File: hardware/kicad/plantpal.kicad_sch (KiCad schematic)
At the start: 0 parts

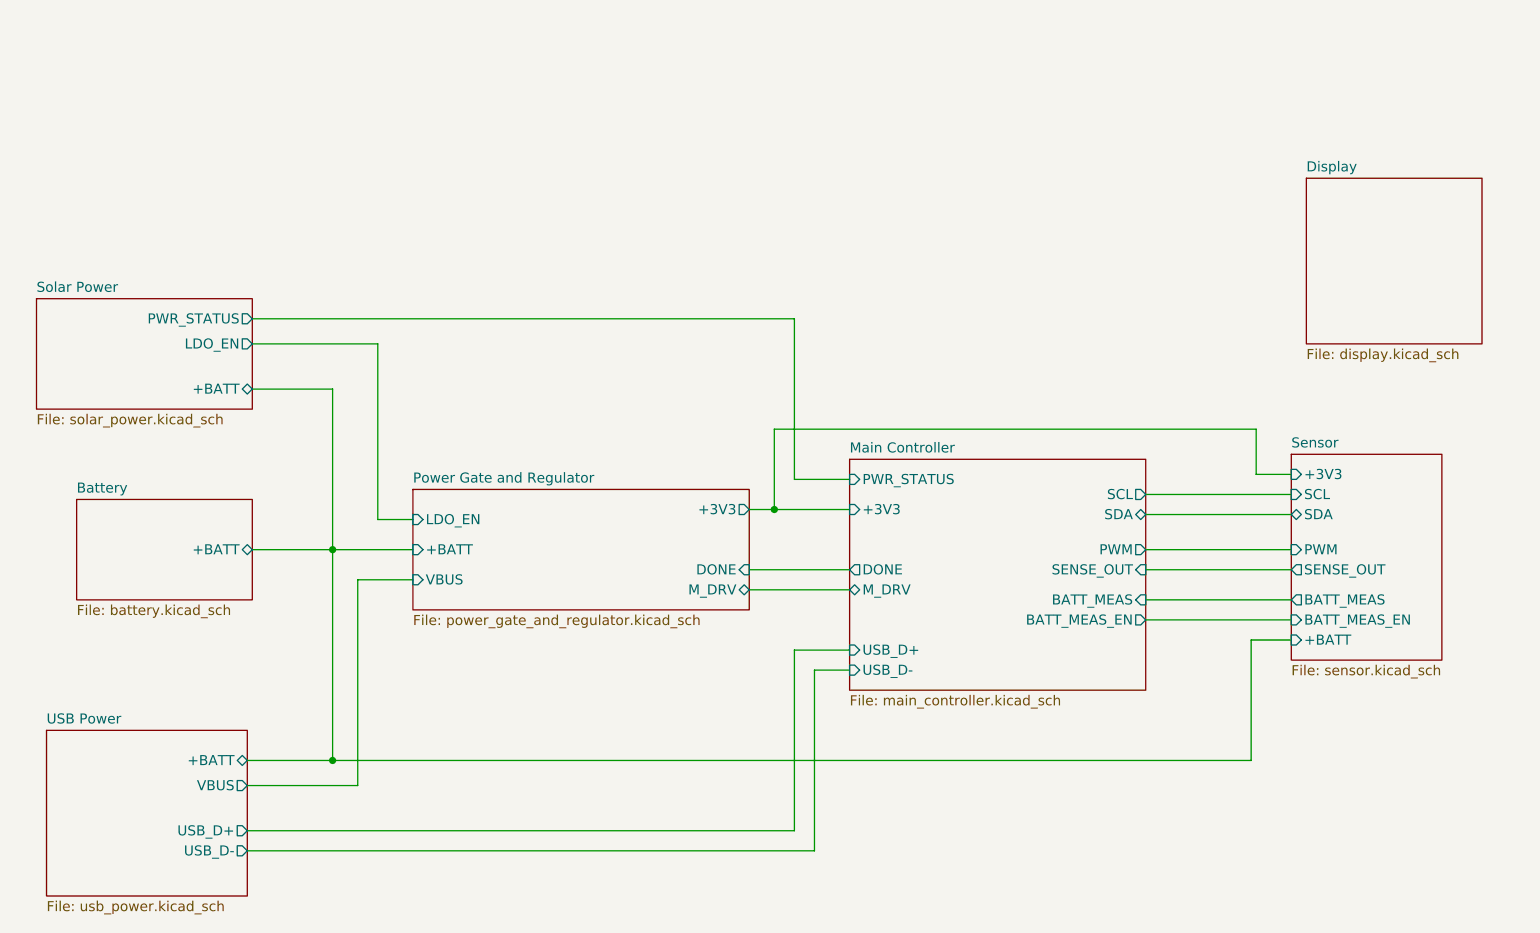
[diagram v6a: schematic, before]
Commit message: first pass schematic and new fpc symbol
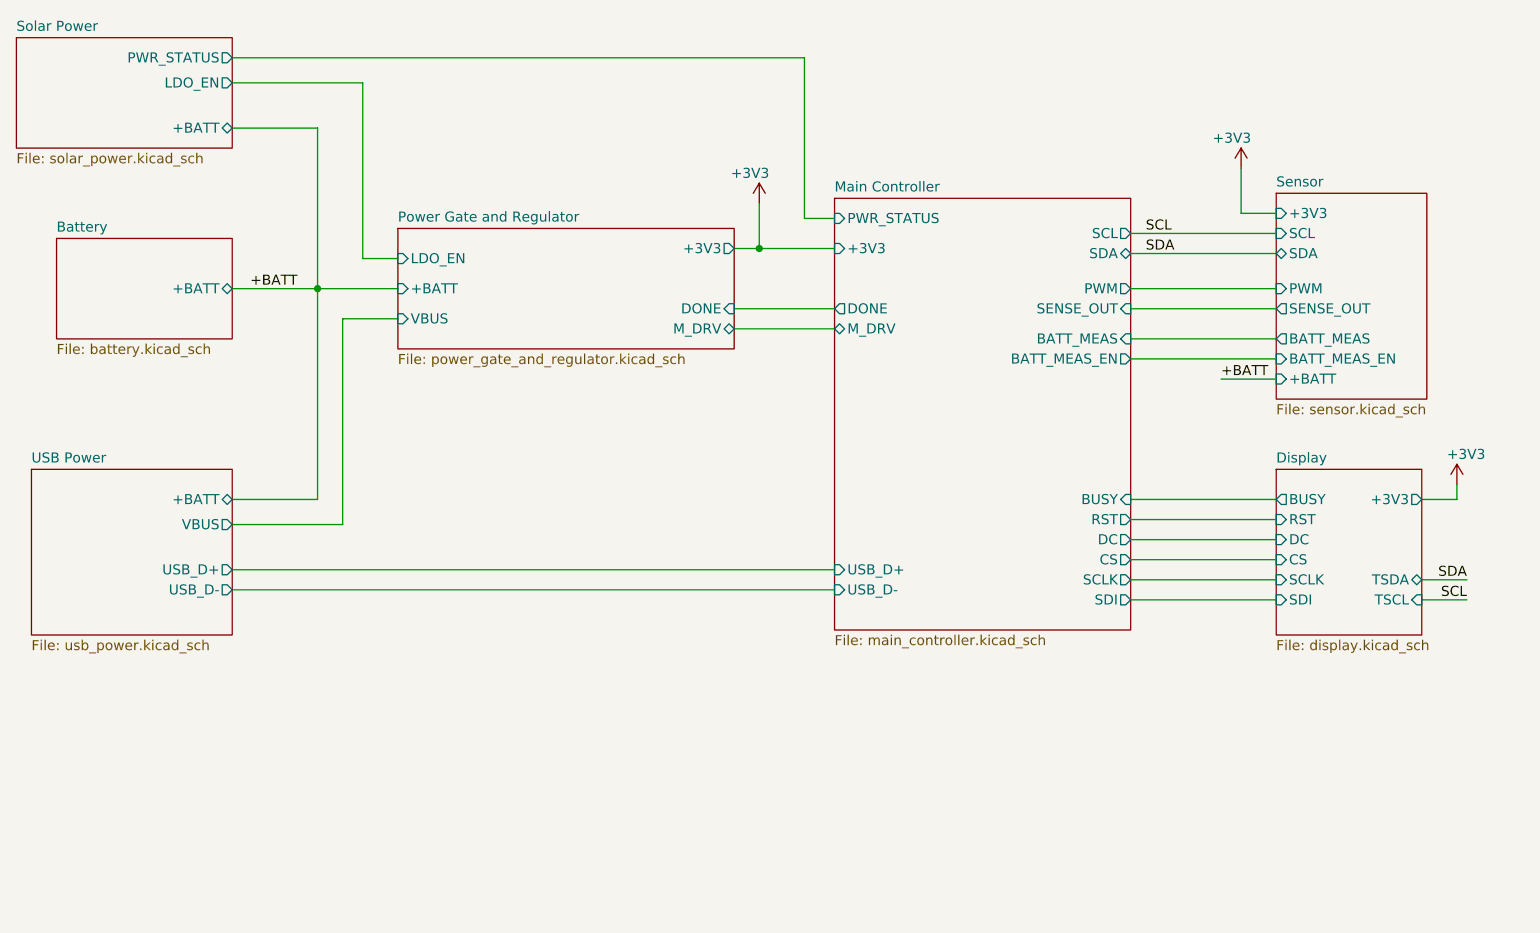
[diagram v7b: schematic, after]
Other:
- sheet Display ports: added +3V3, BUSY, CS, DC, RST, SCLK, SDI, TSCL, TSDA; removed none
- sheet Main Controller ports: added BUSY, CS, DC, RST, SCLK, SDI; removed none
